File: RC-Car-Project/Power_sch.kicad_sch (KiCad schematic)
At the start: 33 parts, among them Q7 PMOS, U1 LMR16020PDDAR, U2 A6986F3V3TR

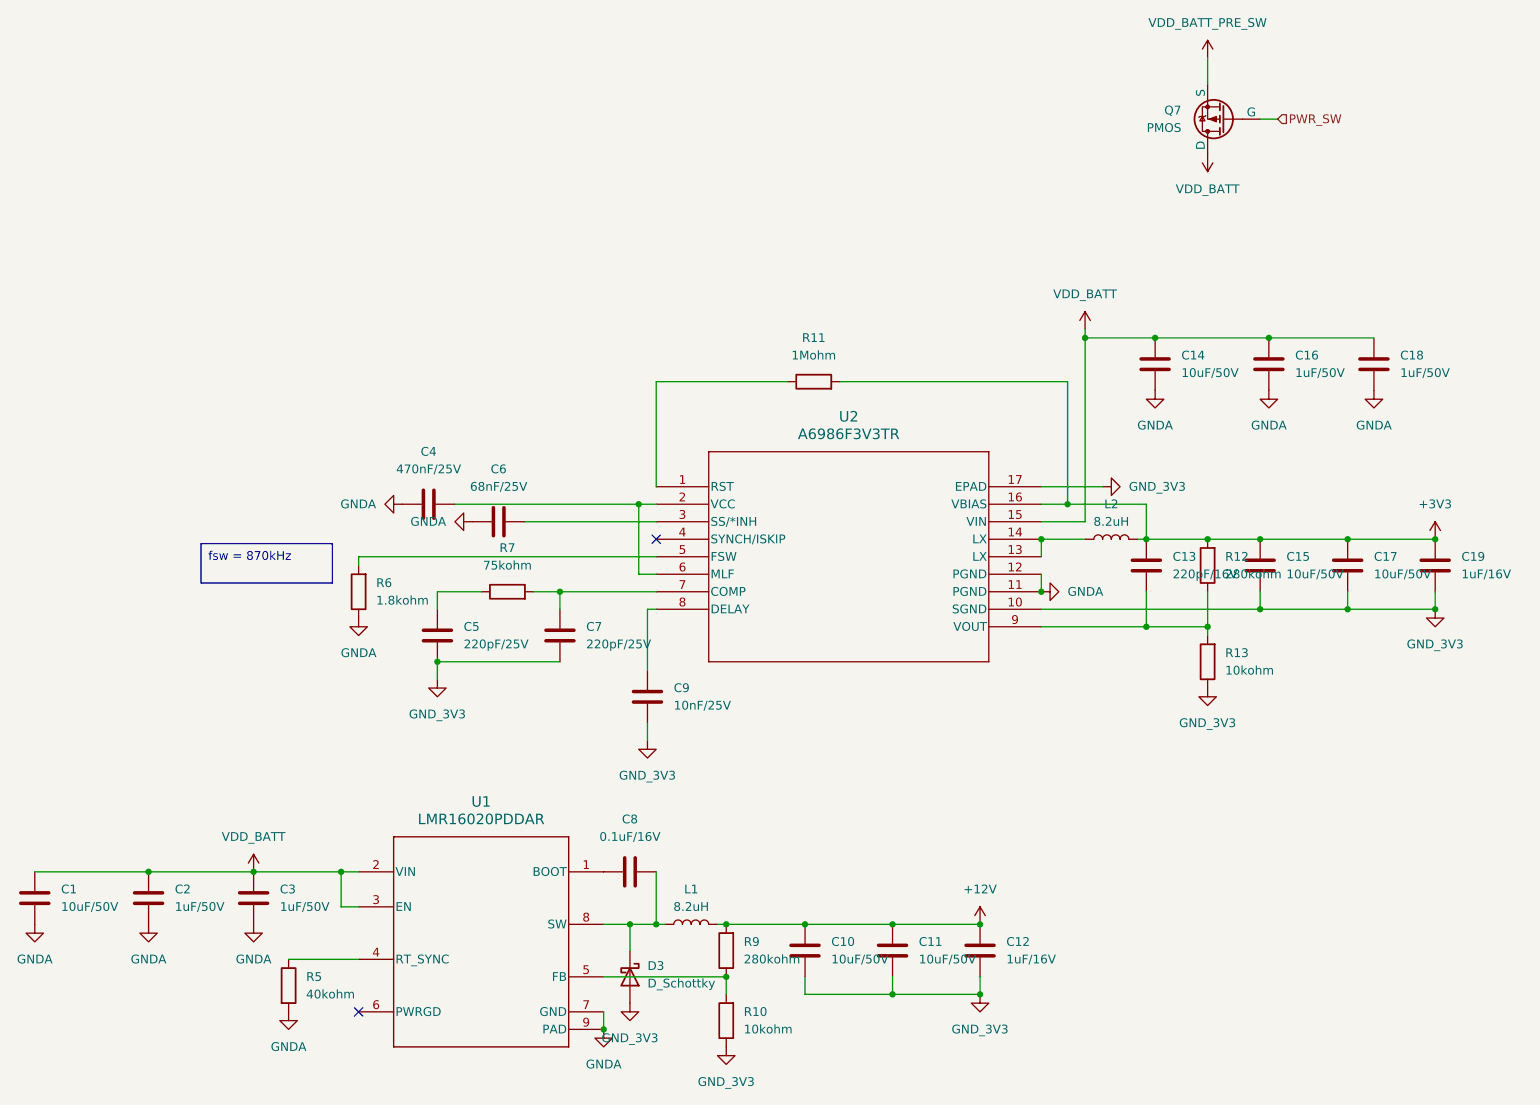
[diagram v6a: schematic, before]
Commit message: Update DC power supply to 3A and 60V
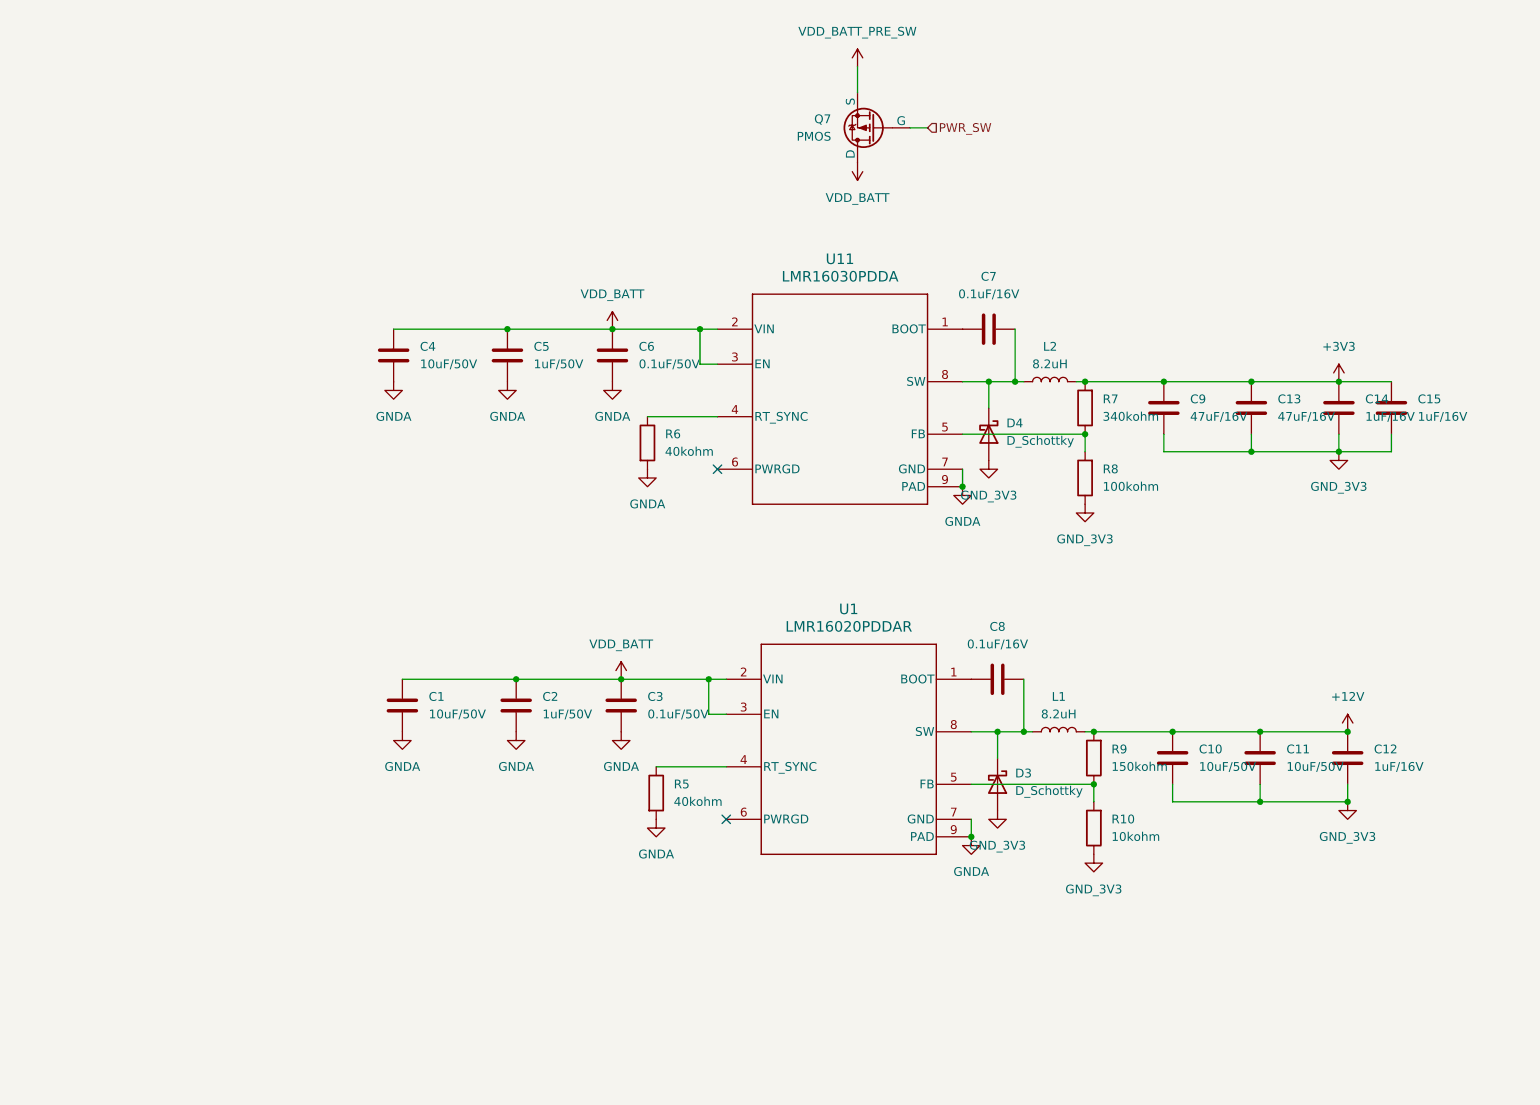
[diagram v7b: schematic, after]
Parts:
- removed C16, C18: 1uF/50V, Capacitor_SMD:C_0603_1608Metric, symbol Device:C
- removed C17: 10uF/50V, Capacitor_SMD:C_0603_1608Metric, symbol Device:C
- removed C19: 1uF/16V, Capacitor_SMD:C_0603_1608Metric, symbol Device:C
- removed R11: 1Mohm, Resistor_SMD:R_0603_1608Metric, symbol Device:R
- removed R12: 280kohm, Resistor_SMD:R_0603_1608Metric, symbol Device:R
- removed R13: 10kohm, Resistor_SMD:R_0603_1608Metric, symbol Device:R
- removed U2: A6986F3V3TR, footprints:HTSSOP16_4P5X5P1X0P65P_STM, symbol A6986F3V3TR:A6986F3V3TR
- added D4: D_Schottky, Diode_SMD:Nexperia_CFP3_SOD-123W, symbol Device:D_Schottky
- added R8: 100kohm, Resistor_SMD:R_0603_1608Metric, symbol Device:R
- added U11: LMR16030PDDA, DDA0008E_N, symbol LMR16030PDDA:LMR16030PDDA
- C13: value 220pF/16V -> 47uF/16V; footprint Capacitor_SMD:C_0603_1608Metric -> Capacitor_SMD:C_0805_2012Metric
- C14, C15: value 10uF/50V -> 1uF/16V
- C3: value 1uF/50V -> 0.1uF/50V
- C4: value 470nF/25V -> 10uF/50V
- C5: value 220pF/25V -> 1uF/50V
- C6: value 68nF/25V -> 0.1uF/50V
- C7: value 220pF/25V -> 0.1uF/16V
- C9: value 10nF/25V -> 47uF/16V; footprint Capacitor_SMD:C_0603_1608Metric -> Capacitor_SMD:C_0805_2012Metric
- R6: value 1.8kohm -> 40kohm
- R7: value 75kohm -> 340kohm
- R9: value 280kohm -> 150kohm
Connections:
- net +3V3: now also C14.1, C9.1, R7.2
- net GNDA: now also C5.2, R6.2, U11.7 (GND), U11.9 (PAD); no longer C14.2, R6.1
- net GND_3V3: now also C13.2, C14.2, D4.2 (A), R8.1; no longer C5.1, C7.1
- net VDD_BATT: now also C4.1, C5.1, C6.1, U11.2 (VIN), U11.3 (EN); no longer C14.1
- net at L2.1: now also C7.1, D4.1 (K), U11.8 (SW)
- net at C7.2: now also U11.1 (BOOT); no longer R7.2
- net at R7.1: now also R8.2, U11.5 (FB); no longer C5.2
- new net: R6.1, U11.4 (RT_SYNC)
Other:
- moved on the sheet: C1, C10, C11, C12, C2, C8, D3, L1, Q7, R10, R5, R9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

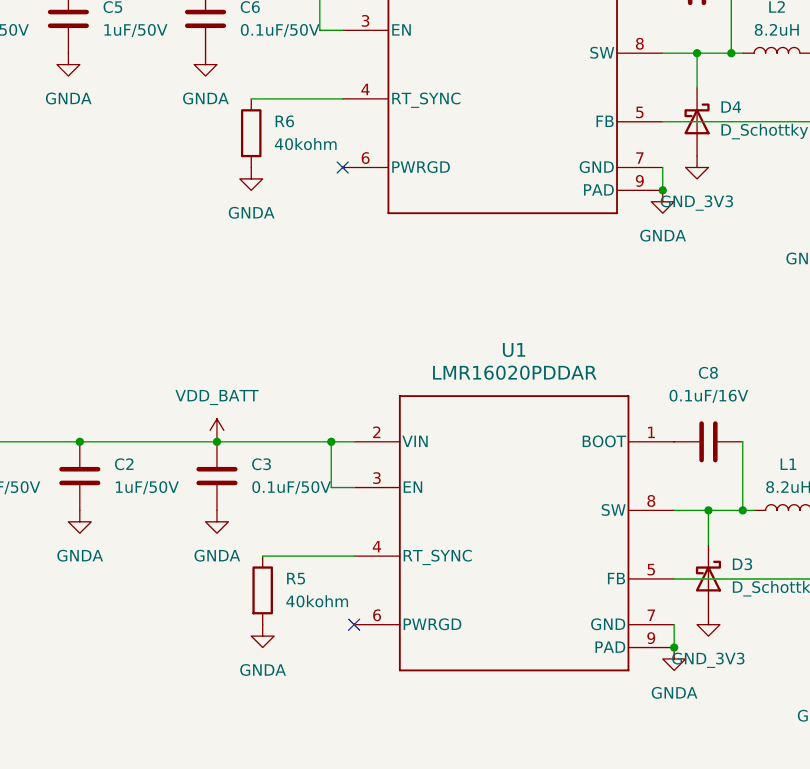
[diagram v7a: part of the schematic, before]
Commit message: Fix power supply layout
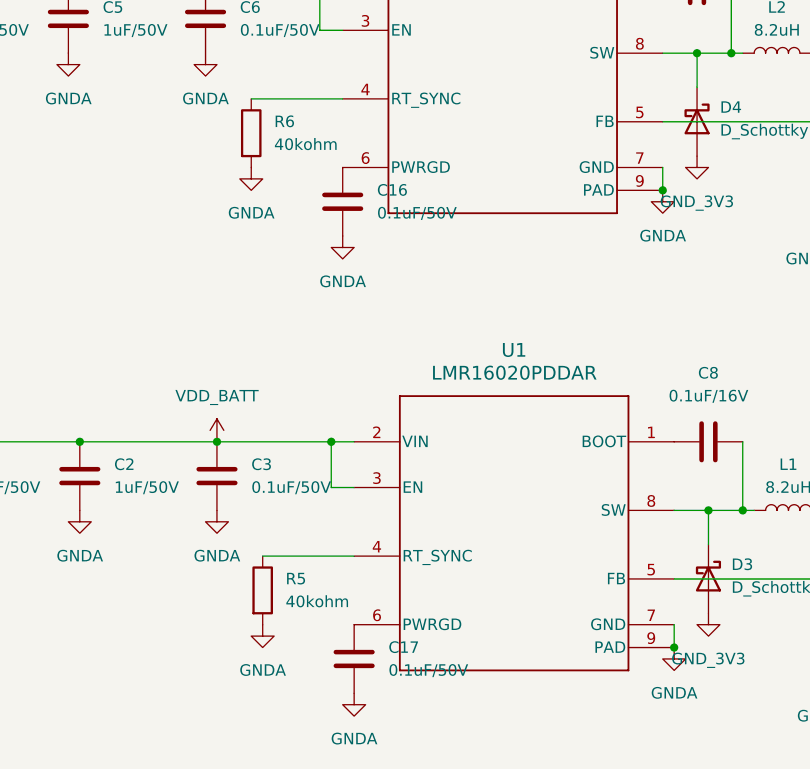
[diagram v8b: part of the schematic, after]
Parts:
- added C16, C17: 0.1uF/50V, Capacitor_SMD:C_0603_1608Metric, symbol Device:C
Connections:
- net GNDA: now also C16.2, C17.2
- net at U1.6 (PWRGD): now also C17.1
- net at U11.6 (PWRGD): now also C16.1
- no-connect marks 2 -> 0
